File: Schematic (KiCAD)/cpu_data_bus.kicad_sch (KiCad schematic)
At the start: 169 parts, among them P13 INVERT, P19 INVERT, P26 INVERT, P5 INVERT, P7 INVERT, X18 INVERT, X19 INVERT, X20 INVERT, X21 INVERT, X22 INVERT, X23 INVERT, X24 INVERT, X25 INVERT, Y11 INVERT, Y12 INVERT, Y18 INVERT, Y19 INVERT, Y25 INVERT, Y26 INVERT, Y4 INVERT, Y5 INVERT

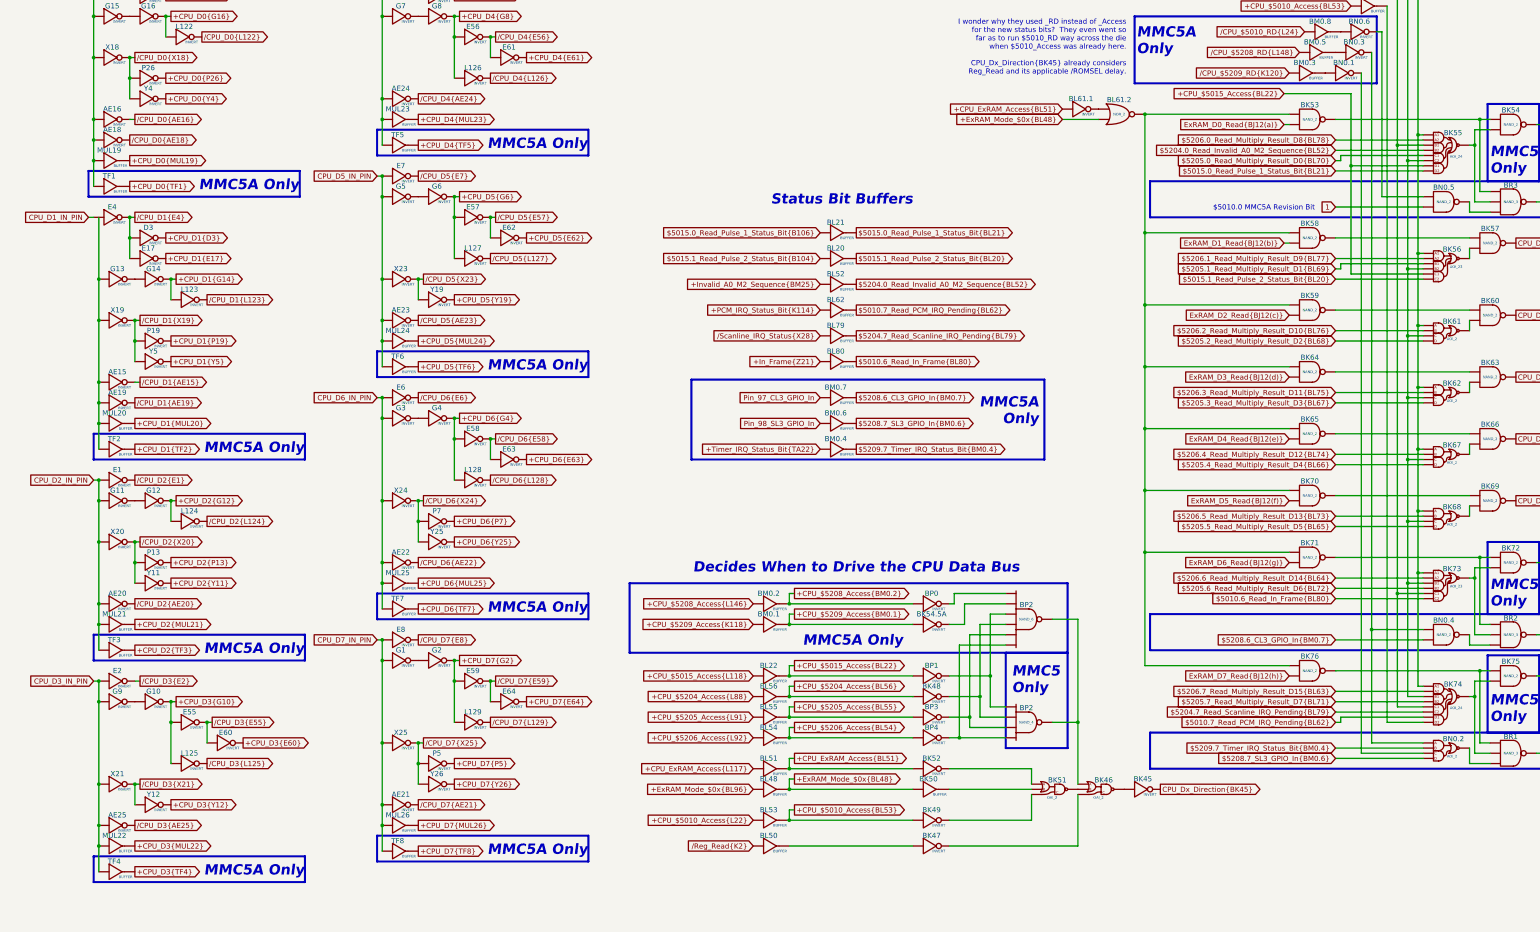
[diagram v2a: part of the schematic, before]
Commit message: - Updated all of the various And-OR-Invert gates to have consistent names.  - Added the schematic for CL3 / SL3 GPIO pins.  There are no surprises revealed by this.  - Finished up the CPU address decoding tracing.  - Added one of the 'artifact' counters from the pulse channels
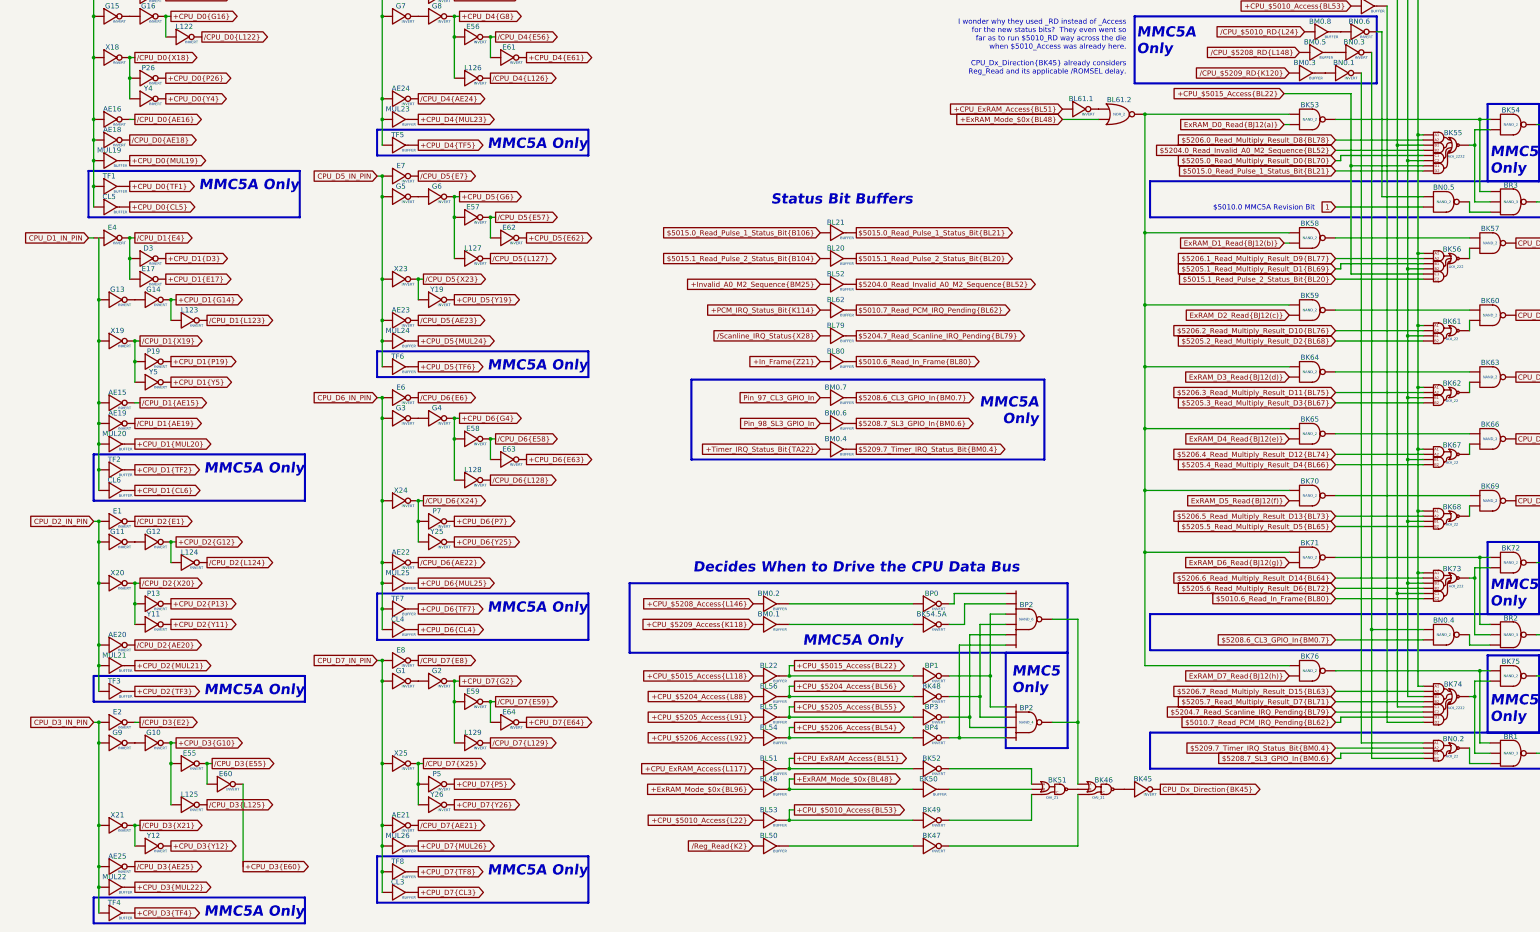
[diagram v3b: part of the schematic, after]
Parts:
- added CL3, CL4, CL5, CL6: BUFFER, symbol MMC5:BUFFER
- BK46, BK51: value OAI_2 -> OAI_21
- BK55, BK74: value AOI_24 -> AOI_2222
- BK56, BK73: value AOI_23 -> AOI_222
- BK61, BK62, BK67, BK68, BN0.2: value AOI_2 -> AOI_22
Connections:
- net CPU_D0_IN_PIN: now also CL5. (X)
- net CPU_D6_IN_PIN: now also CL4. (X)
- net CPU_D7_IN_PIN: now also CL3. (X)
- net at BN0.1. (X): now also BN0.2. (X); no longer BM0.3. (X)
- net at BK47. (X): now also BK46. (X); no longer BL50. (X)
- net at BK46. (X): now also BK45. (X); no longer BK47. (X)
- net at BN0.3. (X): now also BN0.2. (X), BN0.4. (X); no longer BM0.5. (X)
- net at BN0.6. (X): now also BN0.5. (X); no longer BM0.8. (X)
- net at BK51. (X): now also BK49. (X); no longer BK52. (X)
- net +CPU_$5208_Access{BM0.2}: no longer names the net of BM0.2. (X), BP0. (X)
- removed net +CPU_$5209_Access{BM0.1}: BK54.5A. (X), BM0.1. (X)
- new net: BK55. (X), BK56. (X), BK61. (X), BK62. (X), BK67. (X), BK68. (X), BK73. (X), BK74. (X), BL58. (X)
- new net: BK55. (X), BK56. (X), BK61. (X), BK62. (X), BK67. (X), BK68. (X), BK73. (X), BK74. (X), BL59. (X)
- new net: BK66. (X), BK67. (X)
- new net: BK53. (X), BK58. (X), BK59. (X), BK64. (X), BK65. (X), BK70. (X), BK71. (X), BK76. (X), BL61.2. (X)
- new net: BK63. (X), BK64. (X)
- new net: BK69. (X), BK70. (X)
- new net: BK68. (X), BK69. (X)
- new net: BK65. (X), BK66. (X)
- new net: BM0.3. (X), BN0.1. (X)
- new net: BL61.1. (X), BL61.2. (X)
- new net: AE15. (X), AE19. (X), CL6. (X), G13. (X), MUL20. (X), TF2. (X), X19. (X)
- new net: BK57. (X), BK58. (X)
- new net: G15. (X), G16. (X)
- new net: BK75. (X), BK76. (X), BR1. (X)
- new net: G10. (X), G9. (X)
- new net: BK47. (X), BL50. (X)
- new net: G1. (X), G2. (X)
- new net: BM0.5. (X), BN0.3. (X)
- new net: BM0.8. (X), BN0.6. (X)
- new net: G7. (X), G8. (X)
- new net: G11. (X), G12. (X)
- new net: G5. (X), G6. (X)
- new net: BK54.5A. (X), BM0.1. (X)
- new net: BK53. (X), BK54. (X), BR3. (X)
- new net: G3. (X), G4. (X)
- new net: BK48. (X), BP2. (X), BP2. (X)
- new net: BP2. (X), BP2. (X), BP3. (X)
- new net: BK55. (X), BK73. (X), BK74. (X), BL60. (X)
- new net: BK54. (X), BK55. (X), BR3. (X)
- new net: BK72. (X), BK73. (X), BR2. (X)
- new net: BK71. (X), BK72. (X), BR2. (X)
- new net: BK74. (X), BK75. (X), BR1. (X)
- new net: BK74. (X), BL57. (X)
- new net: BK60. (X), BK61. (X)
- new net: BK59. (X), BK60. (X)
- new net: BN0.2. (X), BR1. (X)
- new net: BN0.5. (X), BR3. (X)
- new net: BK56. (X), BK57. (X)
- new net: BN0.4. (X), BR2. (X)
- new net: BP1. (X), BP2. (X), BP2. (X)
- new net: BK46. (X), BP2. (X), BP2. (X)
- new net: BP2. (X), BP2. (X), BP4. (X)
- new net: BK62. (X), BK63. (X)
- new net: BK51. (X), BK52. (X)
- new net: BK50. (X), BK51. (X)
- new net: BK46. (X), BK51. (X)
- new net +CPU_D0{CL5}: CL5. (X)
- new net +CPU_D1{CL6}: CL6. (X)
- new net +CPU_D6{CL4}: CL4. (X)
- new net +CPU_D7{CL3}: CL3. (X)
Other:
- moved on the sheet: AE15, AE19, AE20, AE21, AE25, D3, E1, E17, E2, E4, E55, E59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
